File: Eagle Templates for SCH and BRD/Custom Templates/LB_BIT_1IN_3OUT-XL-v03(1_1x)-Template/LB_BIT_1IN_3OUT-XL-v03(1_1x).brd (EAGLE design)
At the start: 21.4 x 37.6 mm, 25 parts, among them U1 LV321SOT23-5, U2 LV321SOT23-5, U3 LV321SOT23-5

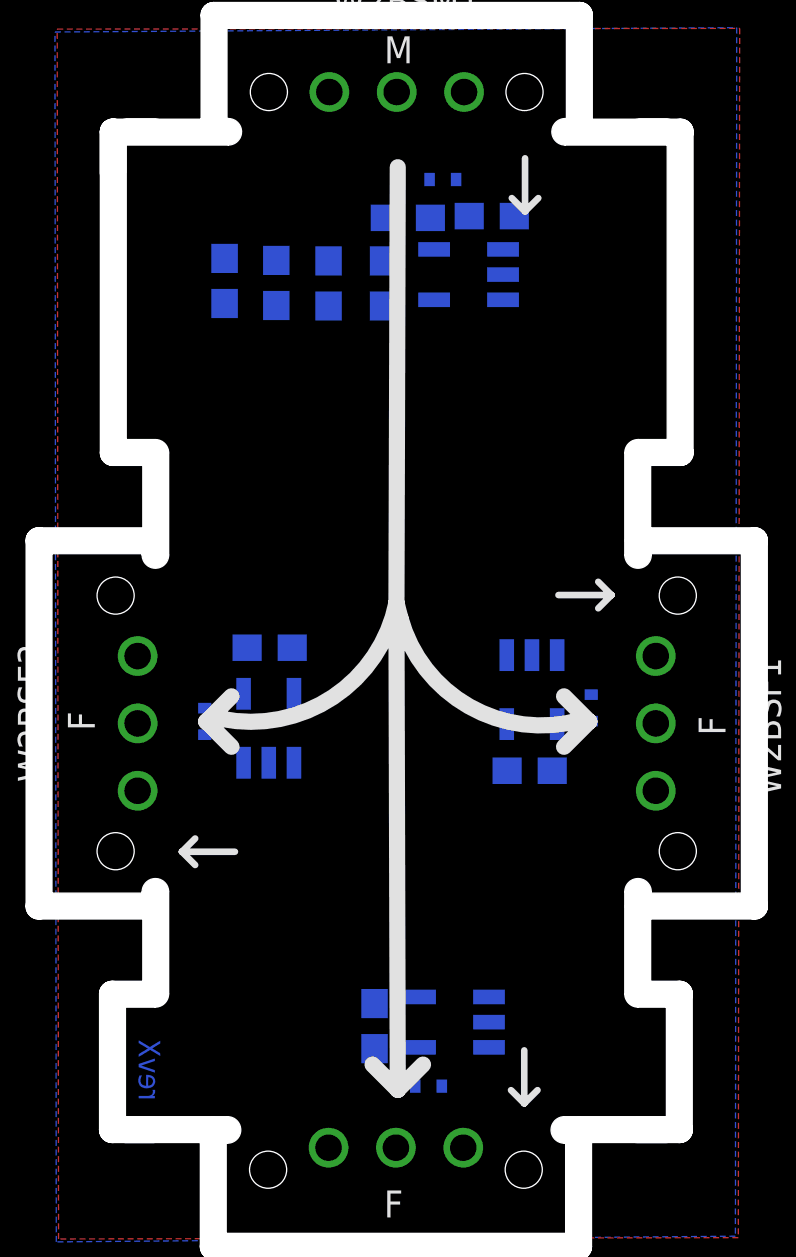
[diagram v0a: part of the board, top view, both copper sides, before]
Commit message: added bitlab logo and made minor changes to board templates. Updated littlebits library.
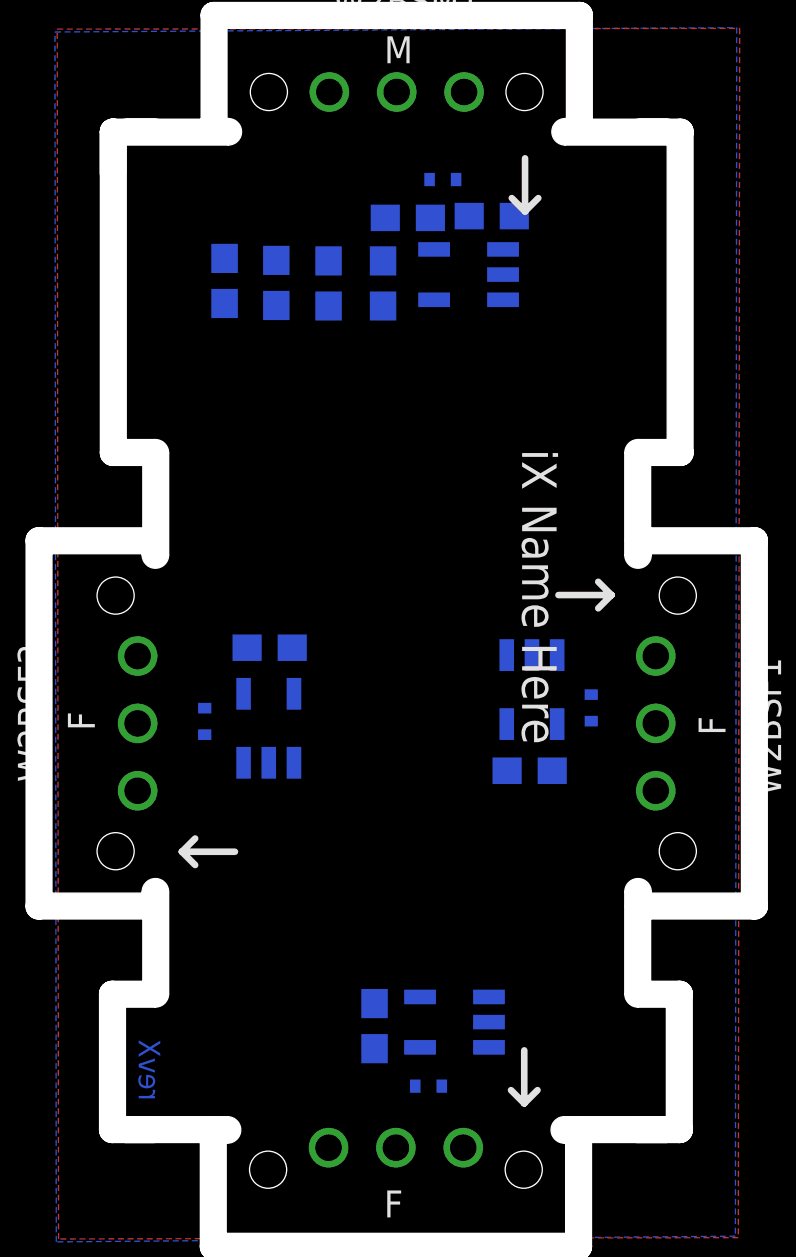
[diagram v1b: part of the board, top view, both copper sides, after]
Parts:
- added U$2: (no value), LITTLEBITS:BITLAB-LOGO
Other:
- board text added: "iX Name Here"
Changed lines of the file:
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@@
 <board>
 <plain>
-<wire x1="13.25" y1="40.79" x2="13.2" y2="24.363" width="0.6096" layer="21"/>
-<wire x1="13.2" y1="24.363" x2="6.6125" y2="19.985" width="0.6096" layer="21" curve="-89.990333"/>
-<wire x1="13.2" y1="24.363" x2="13.35" y2="23.786" width="0.6096" layer="21"/>
-<wire x1="13.35" y1="23.786" x2="20.12" y2="19.935" width="0.6096" layer="21" curve="90"/>
-<wire x1="6.6125" y1="19.985" x2="6.0275" y2="19.885" width="0.6096" layer="21"/>
-<wire x1="6.0275" y1="19.885" x2="6.98" y2="20.8375" width="0.6096" layer="21"/>
-<wire x1="6.0275" y1="19.885" x2="6.98" y2="18.9325" width="0.6096" layer="21"/>
-<wire x1="20.4725" y1="19.885" x2="19.52" y2="20.8375" width="0.6096" layer="21"/>
-<wire x1="20.12" y1="19.935" x2="20.4725" y2="19.885" width="0.6096" layer="21"/>
-<wire x1="20.4725" y1="19.885" x2="19.52" y2="18.9325" width="0.6096" layer="21"/>
-<wire x1="13.2" y1="23.955" x2="13.25" y2="5.9975" width="0.6096" layer="21"/>
-<wire x1="13.25" y1="5.9975" x2="12.2975" y2="6.95" width="0.6096" layer="21"/>
-<wire x1="13.25" y1="5.9975" x2="14.2025" y2="6.95" width="0.6096" layer="21"/>
 <wire x1="2.98" y1="9.115" x2="2.98" y2="4.985" width="0" layer="20"/>
 <wire x1="23.38" y1="9.115" x2="23.38" y2="4.985" width="0" layer="20"/>
@@
 <dimension x1="0.21" y1="13.415" x2="26.21" y2="13.415" x3="13.21" y3="-4.13" textsize="1.778" layer="114"/>
 <text x="3.48" y="5.585" size="0.8128" layer="16" font="vector" ratio="12" rot="MR90">revX</text>
+<text x="18.59" y="24.59" size="1.3" layer="21" font="vector" rot="SR270" align="center">iX Name Here</text>
 </plain>
 <attributes>
@@
 <element name="U$1" library="LITTLEBITS" package="OSHWCREDIT" value="OSHWCREDIT" x="-92.37" y="-61.97"/>
 <element name="FRAME1" library="LITTLEBITS" package="FABDWG01-OHW" value="FRAME-LETTER" x="0" y="0"/>
+<element name="U$2" library="LITTLEBITS" package="BITLAB-LOGO" value="" x="17.165" y="28.13" rot="R270"/>
 </elements>
 <signals>

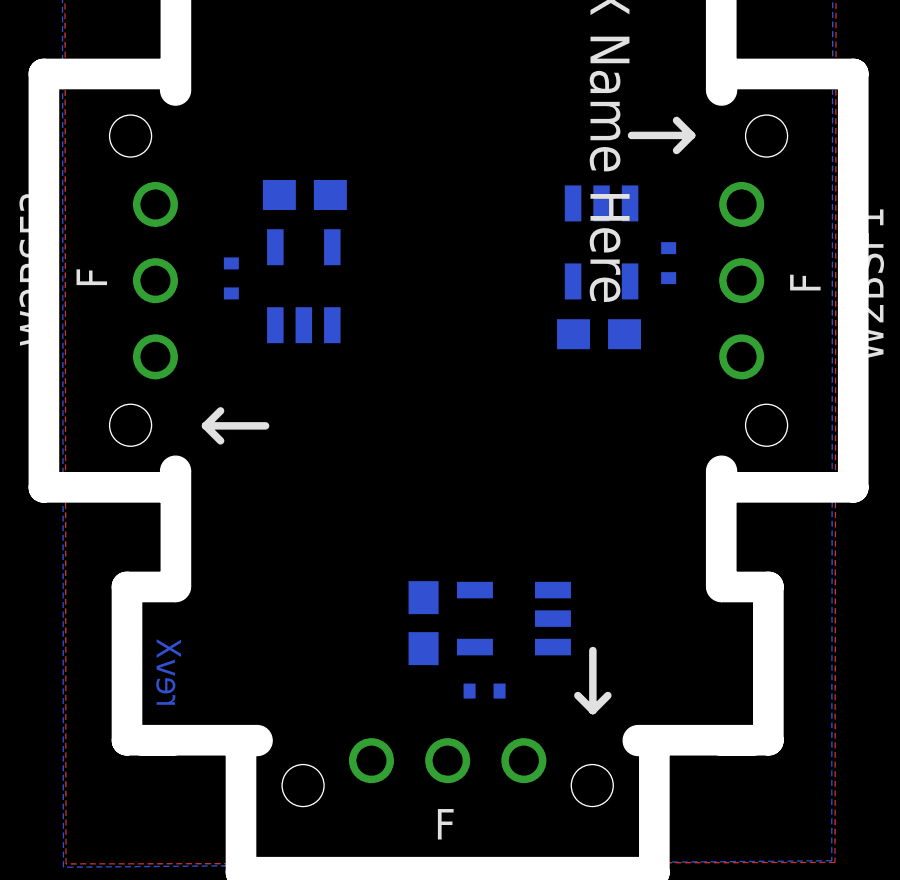
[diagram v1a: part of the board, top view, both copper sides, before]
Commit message: Moved output stages which were placed next to the wrong bitsnaps
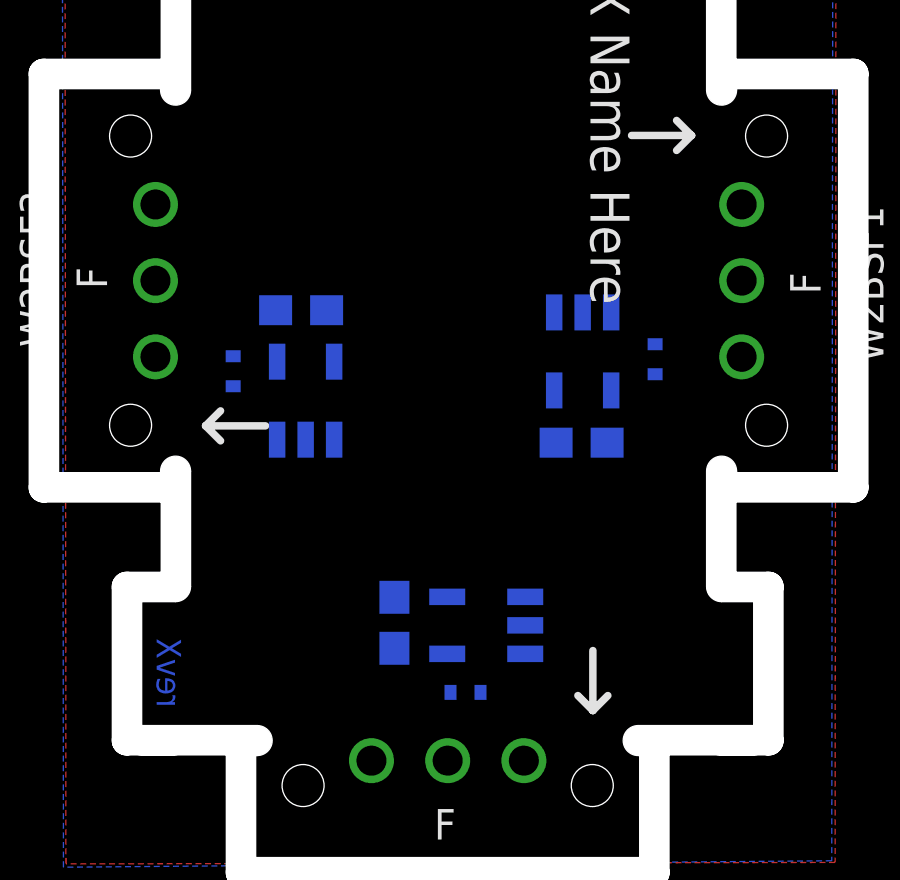
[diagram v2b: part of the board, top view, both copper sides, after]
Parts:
- moved I?TVS1 15.8 mm to (13.8, 6.09), turned to 0 degrees
- moved I?TVS2 14.4 mm to (20.1, 17.2), turned to 90 degrees
- moved I?TVS3 13.6 mm to (6.03, 16.8), turned to 90 degrees
- moved U1 13.3 mm to (14.5, 8.32), turned to 270 degrees
- moved I?C5 12.4 mm to (17.6, 14.4), turned to 0 degrees
- moved I?C4 11.8 mm to (11.4, 8.41), turned to 90 degrees
- moved I?C3 11.2 mm to (8.29, 18.8), turned to 180 degrees
- moved U3 10.1 mm to (8.45, 15.8), turned to 0 degrees
- moved U2 9.55 mm to (17.7, 17.5), turned to 180 degrees

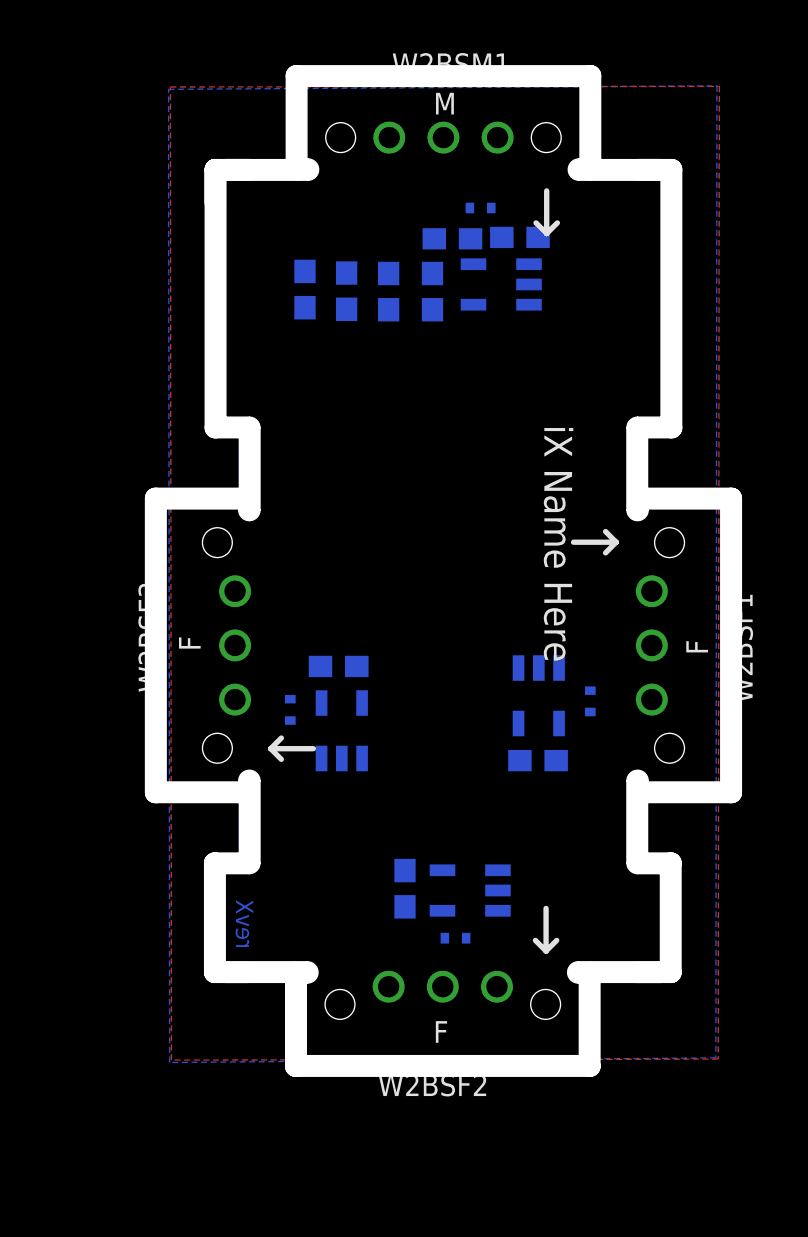
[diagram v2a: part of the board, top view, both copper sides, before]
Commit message: Updated templates
- Added ferrite beads
- Moved text and annotations off of Nets layer
- Minor layout changes
- Removed I/O/W prefix from reference designators
- Removed output stage components from output bits
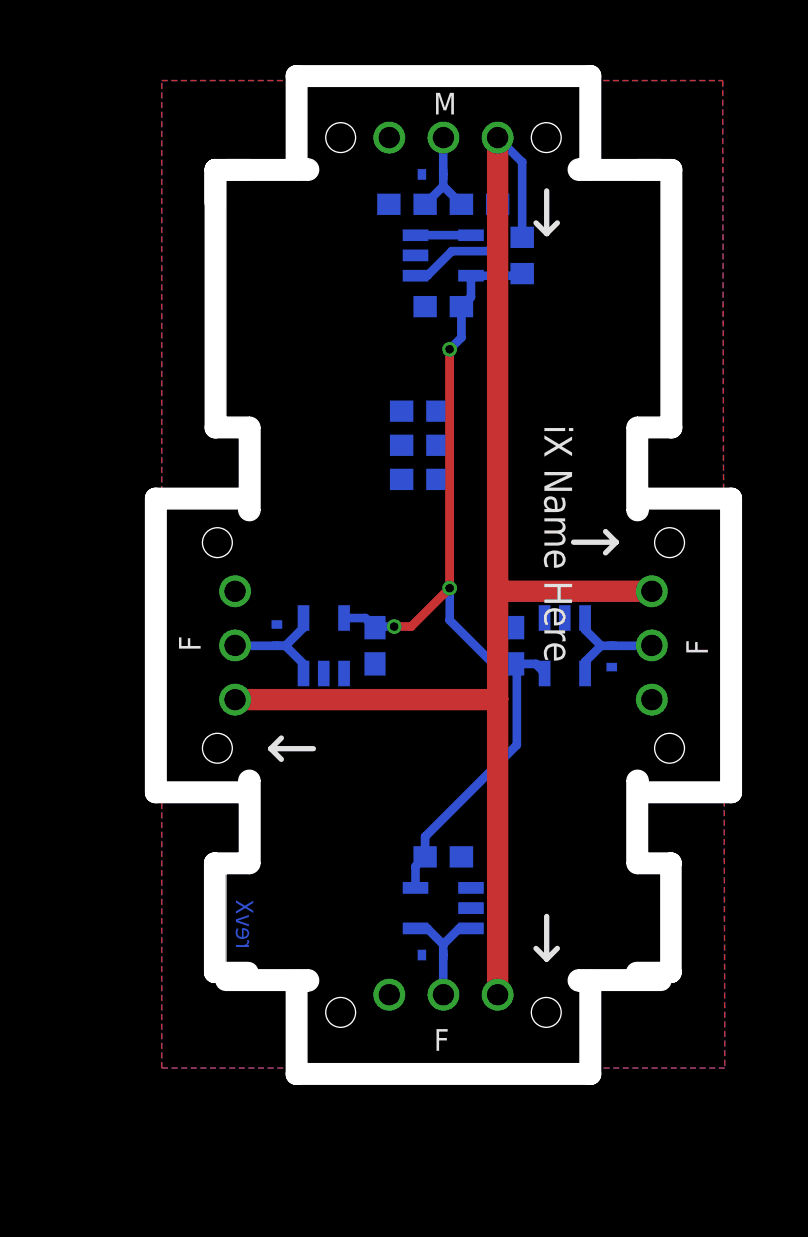
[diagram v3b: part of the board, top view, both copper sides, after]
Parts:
- removed I?C1: 0.1uF, LITTLEBITS:CAP-0603
- removed I?C2: 10uF, LITTLEBITS:CAP-0603
- removed I?C3, I?C4, I?C5: 1.0uF, LITTLEBITS:CAP-0603
- removed I?R3, I?R4: 3K3, LITTLEBITS:RES-0603
- removed I?TVS1, I?TVS2, I?TVS3, W2TVS1: ESD9B5.0ST5G, LITTLEBITS:SOD-923
- removed W2BSF2: BITSNAP_V03_FEMALE, bitSnap:BITSNAP_V03_FEMALE
- removed W2R1: 1meg, LITTLEBITS:RES-0603
- removed W2R2: 10k, LITTLEBITS:RES-0603
- removed W2U1: LV321SOT23-5, LITTLEBITS:SOT23-5
- added BSF2: BITSNAP_V03_FEMALE, bitSnap:BITSNAP_V03_FEMALE
- added C1: 0.1uF, LITTLEBITS:CAP-0603
- added C2: 10uF, LITTLEBITS:CAP-0603
- added C3, C4, C5: 1.0uF, LITTLEBITS:CAP-0603
- added FB1: FERRITE-BEAD0603, LITTLEBITS:R0603
- added R1: 1meg, LITTLEBITS:RES-0603
- added R2: 10k, LITTLEBITS:RES-0603
- added R3, R4: 3K3, LITTLEBITS:RES-0603
- added TVS1, TVS2, TVS3, TVS4: (no value), LITTLEBITS:SOD-923
- added U4: LV321SOT23-5, LITTLEBITS:SOT23-5
- moved U1 29.8 mm to (13.2, 38.1), turned to 90 degrees
- moved U2 10.3 mm to (7.60, 19.8), turned to 0 degrees
- moved U3 9.58 mm to (13.2, 7.50), turned to 270 degrees
- renumbered W2BSF1 to BSF3, W2BSF3 to BSF1, W2BSM to BSM1
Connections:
- removed net N$1 (its old number): U1.1
- new net LB_VCC: BSF1.VCC, BSF2.VCC, BSF3.VCC, BSM1.VCC1, FB1.2
- new net N$5: U4.1
- net GND: now also BSF2.GND, C1.2, C2.2, C3.1, C4.1, C5.1, R1.1, R4.1, TVS1.1, TVS2.1, TVS3.1, TVS4.1, U4.2; no longer I?C1.2, I?C2.2, I?C3.1, I?C4.1, I?C5.1, I?R4.1, I?TVS1.1, I?TVS2.1, I?TVS3.1, W2BSF2.GND, W2R1.1, W2TVS1.1, W2U1.2
- net N$2: now also U1.3, U1.4; no longer W2U1.3, W2U1.4
- net N$3: now also R2.2, U1.1; no longer W2R2.2, W2U1.1
- net SIG_IN: now also R1.2, R2.1, TVS1.2; no longer W2R1.2, W2R2.1, W2TVS1.2
- net SIG_OUT1: now also TVS2.2, U2.3, U2.4; no longer I?TVS3.2, U3.3, U3.4
- net SIG_OUT2: now also BSF2.SIG, TVS3.2, U3.3, U3.4; no longer I?TVS1.2, U1.3, U1.4, W2BSF2.SIG
- net SIG_OUT3: now also TVS4.2, U4.3, U4.4; no longer I?TVS2.2, U2.3, U2.4
- net VCC: now also C1.1, C3.2, C4.2, C5.2, FB1.1, R3.2, U4.5; no longer BSF1.VCC, BSF3.VCC, BSM1.VCC1, I?C1.1, I?C3.2, I?C4.2, I?C5.2, I?R3.2, W2BSF2.VCC, W2U1.5
- net VREF: now also C2.1, R3.1, R4.2; no longer I?C2.1, I?R3.1, I?R4.2
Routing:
- net LB_VCC: track 0.00 -> 65.0 mm
- net VCC: track 0.08 -> 42.9 mm, vias 0 -> 3
- net N$3: track 0.00 -> 6.26 mm
- net SIG_OUT1: track 0.00 -> 5.67 mm
- net SIG_OUT3: track 0.00 -> 5.61 mm
- net SIG_OUT2: track 0.00 -> 5.59 mm
- net SIG_IN: track 0.00 -> 4.69 mm
- net N$2: track 0.00 -> 2.60 mm
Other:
- outline, holes or cut-outs redrawn
- board text removed: "W2BSF1"
- board text removed: "W2BSF2"
- board text removed: "W2BSF3"
- board text removed: "W2BSM1"
